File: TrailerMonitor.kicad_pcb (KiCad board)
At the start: 4 copper layers, 25 parts, among them U2 INA260AIPWR, U3 INA260AIPWR, U4 INA260AIPWR, U5 INA260AIPWR, U6 INA260AIPWR, U7 INA260AIPWR, U8 INA260AIPWR, U9 INA260AIPWR

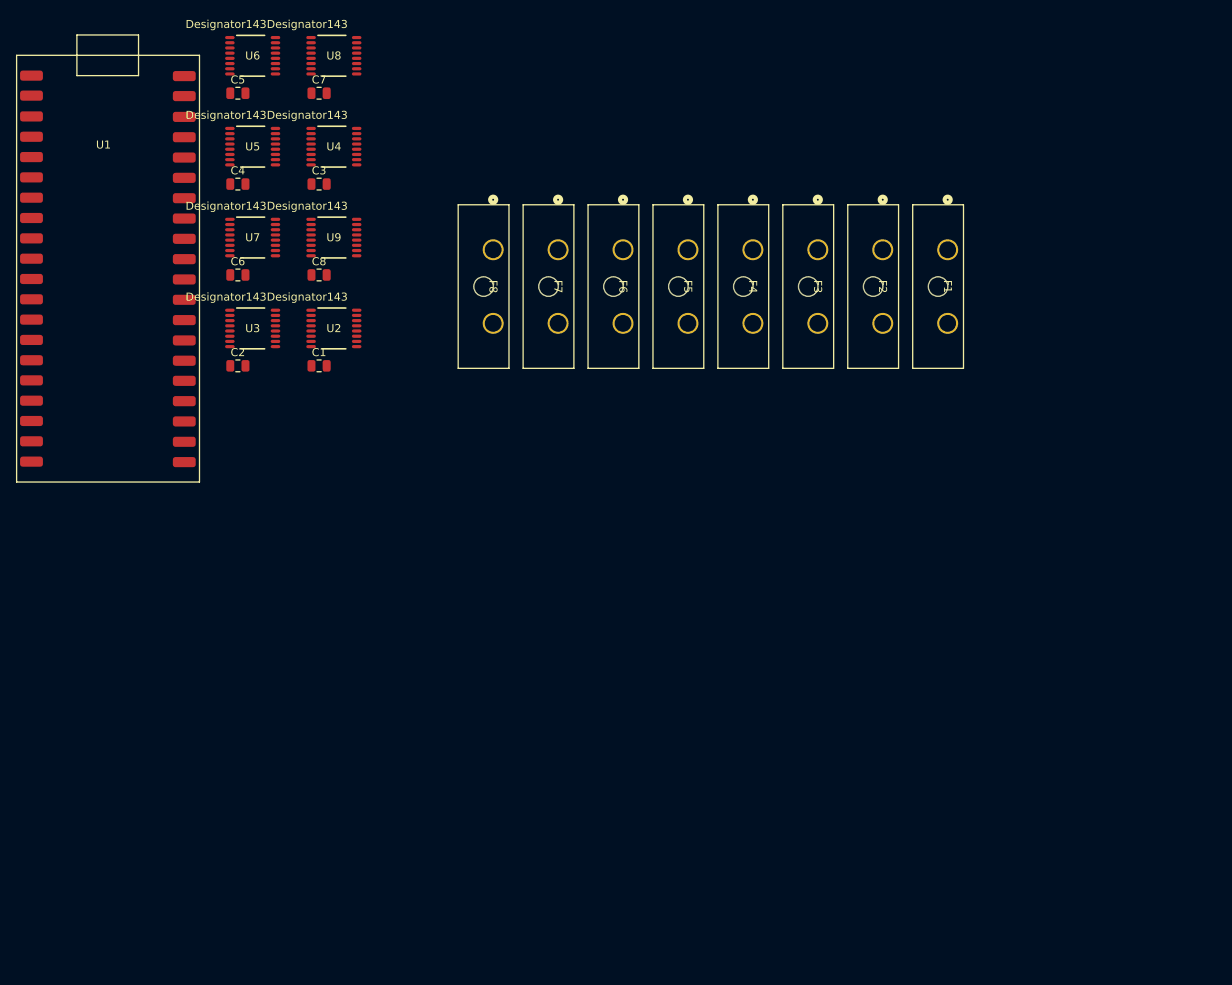
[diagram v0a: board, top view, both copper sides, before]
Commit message: Initial layout; remove INA260
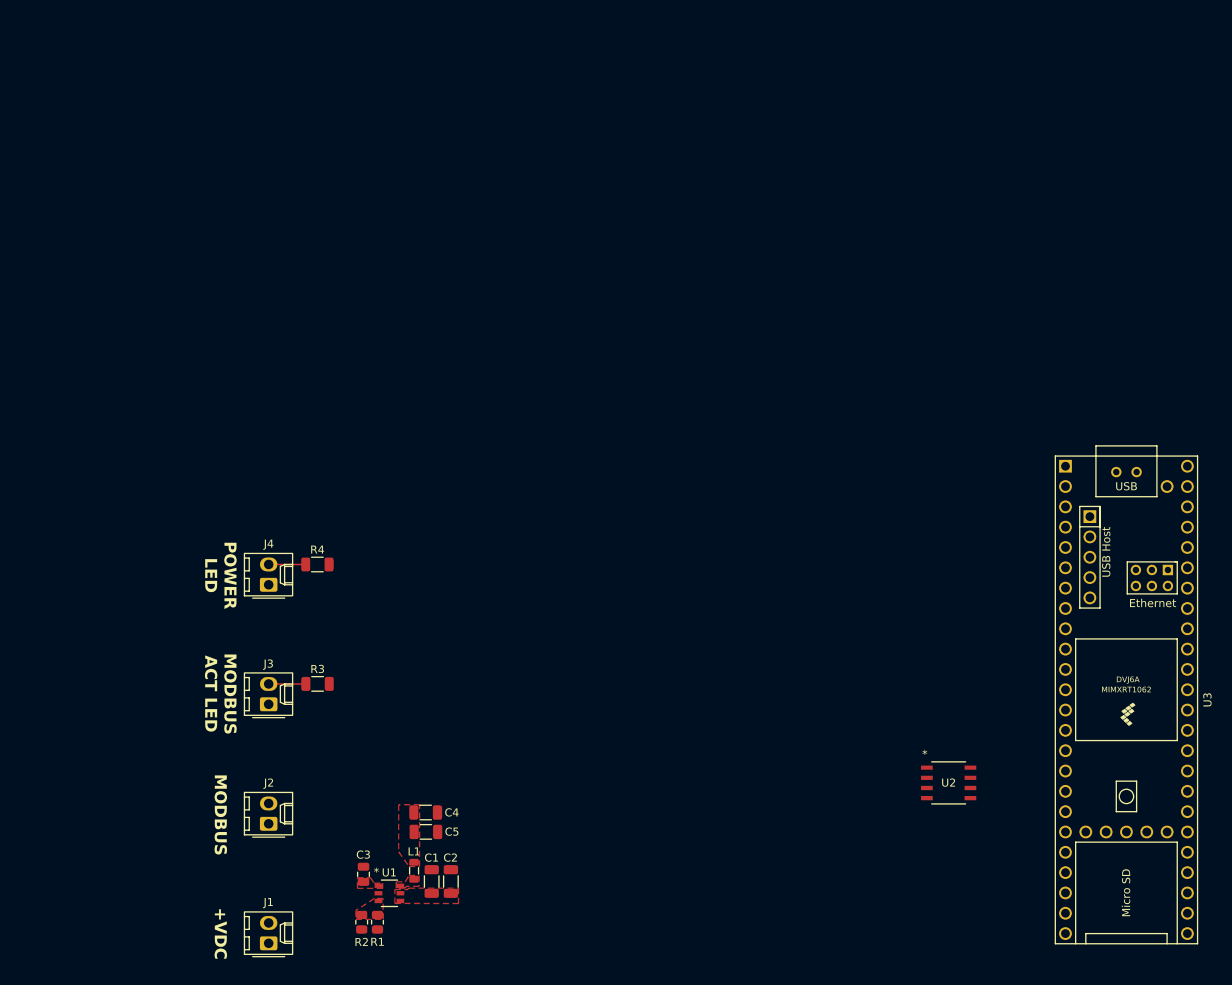
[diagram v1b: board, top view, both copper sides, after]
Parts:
- removed C6, C7, C8: 0.1u, Capacitor_SMD:C_0805_2012Metric
- removed F1, F2, F3, F4, F5, F6, F7, F8: 178.6164.0002, 178_6164_0002:FUSE_178-6164_LTF
- removed U4, U5, U6, U7, U8, U9: INA260AIPWR, INA260AIPWR:PW0016A_L
- added J1: +VIN (7-60 VDC), Connector_Molex:Molex_KK-254_AE-6410-02A_1x02_P2.54mm_Vertical, F.Cu at (153.9, 171.9)
- added J2: ModBus, Connector_Molex:Molex_KK-254_AE-6410-02A_1x02_P2.54mm_Vertical, F.Cu at (153.9, 157.0)
- added J3: LED (Power), Connector_Molex:Molex_KK-254_AE-6410-02A_1x02_P2.54mm_Vertical, F.Cu at (153.9, 142.0)
- added J4: LED (ModBus Act), Connector_Molex:Molex_KK-254_AE-6410-02A_1x02_P2.54mm_Vertical, F.Cu at (153.9, 127.1)
- added L1: 47u, Inductor_SMD:L_0805_2012Metric, F.Cu at (172.1, 162.8)
- added R1: 100k, Resistor_SMD:R_0805_2012Metric, F.Cu at (167.6, 169.3)
- added R2: 19k1, Resistor_SMD:R_0805_2012Metric, F.Cu at (165.6, 169.3)
- added R3: 160, Resistor_SMD:R_1206_3216Metric, F.Cu at (160.1, 139.5)
- added R4: 160, Resistor_SMD:R_1206_3216Metric, F.Cu at (160.0, 124.5)
- C1, C5: value 0.1u -> 4u7; footprint Capacitor_SMD:C_0805_2012Metric -> Capacitor_SMD:C_1206_3216Metric
- C2: value 0.1u -> 100n; footprint Capacitor_SMD:C_0805_2012Metric -> Capacitor_SMD:C_1206_3216Metric
- C3: value 0.1u -> 100n
- C4: value 0.1u -> 10u; footprint Capacitor_SMD:C_0805_2012Metric -> Capacitor_SMD:C_1206_3216Metric
- U1: value ~ -> LMR51606XDBVR; footprint rpi-pico2w:Raspberrypi pico2 w SMD -> LMR51606:SOT-23-6-DBV_TEX
- U2: value INA260AIPWR -> MAX485ESA+; footprint INA260AIPWR:PW0016A_L -> MAX485ESA:21-0041B_8_MXM
- U3: value INA260AIPWR -> Teensy4.1; footprint INA260AIPWR:PW0016A_L -> teensy:Teensy41
- moved U3 118.7 mm to (261.2, 141.5), turned to -90 degrees
- moved U2 95.6 mm to (238.9, 151.8)
- moved C5 95.3 mm to (173.6, 158.0)
- moved U1 92.4 mm to (169.0, 165.7)
- moved C3 86.5 mm to (165.8, 163.3), turned to -90 degrees
- moved C4 82.0 mm to (173.6, 155.6)
- moved C2 69.7 mm to (176.7, 164.2), turned to 90 degrees
- moved C1 66.0 mm to (174.3, 164.2), turned to 90 degrees
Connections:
- C1 pad 1: GND -> +VDC
- C1 pad 2: /INA260/SOURCE -> GND
- C2 pad 1: GND -> +VDC
- C2 pad 2: /INA261/SOURCE -> GND
- C3 pad 1: GND -> Net-(U1-SW)
- C3 pad 2: /INA262/SOURCE -> Net-(U1-CB)
- C4 pad 1: GND -> +5V
- C4 pad 2: /INA263/SOURCE -> GND
- C5 pad 1: GND -> +5V
- C5 pad 2: /INA264/SOURCE -> GND
- U1 pad 1: unconnected-(U1-GP0/I2C0_SDA/UART0_TX-Pad1) -> Net-(U1-CB)
- U1 pad 2: unconnected-(U1-GP1_/I2C0_SCL/UART0_RX-Pad2) -> GND
- U1 pad 3: GND -> Net-(U1-FB)
- U1 pad 4: unconnected-(U1-GP2/SPIO_SCK/I2C1_SDA-Pad4) -> +VDC
- U1 pad 5: unconnected-(U1-GP3/SPIO_TX/I2C1SCL-Pad5) -> +VDC
- U1 pad 6: unconnected-(U1-GP4/SPIO_RX/I2C0_SDA/_UART1_TX-Pad6) -> Net-(U1-SW)
- U2 pad 1: /INA260/SOURCE -> /RO
- U2 pad 2: /INA260/SOURCE -> /DE
- U2 pad 3: /INA260/SOURCE -> /DE
- U2 pad 4: /INA260/A1 -> /DI
- U2 pad 5: /INA260/A0 -> GND
- U2 pad 6: GND -> /A
- U2 pad 7: unconnected-(U2-ALERT-Pad7) -> /B
- U2 pad 8: /SDA0 -> +5V
- U3 pad 1: /INA261/SOURCE -> GND
- U3 pad 10: /INA261/SOURCE -> /DI
- U3 pad 11: GND -> unconnected-(U3-9_OUT1C-Pad11)
- U3 pad 12: /INA261/SOURCE -> unconnected-(U3-10_CS_MQSR-Pad12)
- U3 pad 14: /INA261/LOAD -> unconnected-(U3-12_MISO_MQSL-Pad14)
- U3 pad 15: /INA261/LOAD -> unconnected-(U3-3V3-Pad15)
- U3 pad 16: /INA261/LOAD -> unconnected-(U3-24_A10_TX6_SCL2-Pad16)
- U3 pad 2: /INA261/SOURCE -> unconnected-(U3-0_RX1_CRX2_CS1-Pad2)
- U3 pad 3: /INA261/SOURCE -> unconnected-(U3-1_TX1_CTX2_MISO1-Pad3)
- U3 pad 4: /INA261/A1 -> unconnected-(U3-2_OUT2-Pad4)
- U3 pad 5: /INA261/A0 -> unconnected-(U3-3_LRCLK2-Pad5)
- U3 pad 6: GND -> unconnected-(U3-4_BCLK2-Pad6)
- U3 pad 8: /SDA0 -> /DE
- U3 pad 9: /SCL0 -> /RO
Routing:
- net Net-(J4-Pin_2): track 0.00 -> 4.63 mm
- net Net-(J3-Pin_2): track 0.00 -> 4.43 mm
- added copper zone on F.Cu, net +5V
- added copper zone on F.Cu, net +VDC
- added copper zone on F.Cu, net Net-(U1-CB)
- added copper zone on F.Cu, net Net-(U1-FB)
- added copper zone on F.Cu, net Net-(U1-SW)
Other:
- board text added: "+VDC"
- board text added: "MODBUS"
- board text added: "MODBUS ACT LED"
- board text added: "POWER LED"

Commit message: Add VBUS/VSYS; final PCB layout
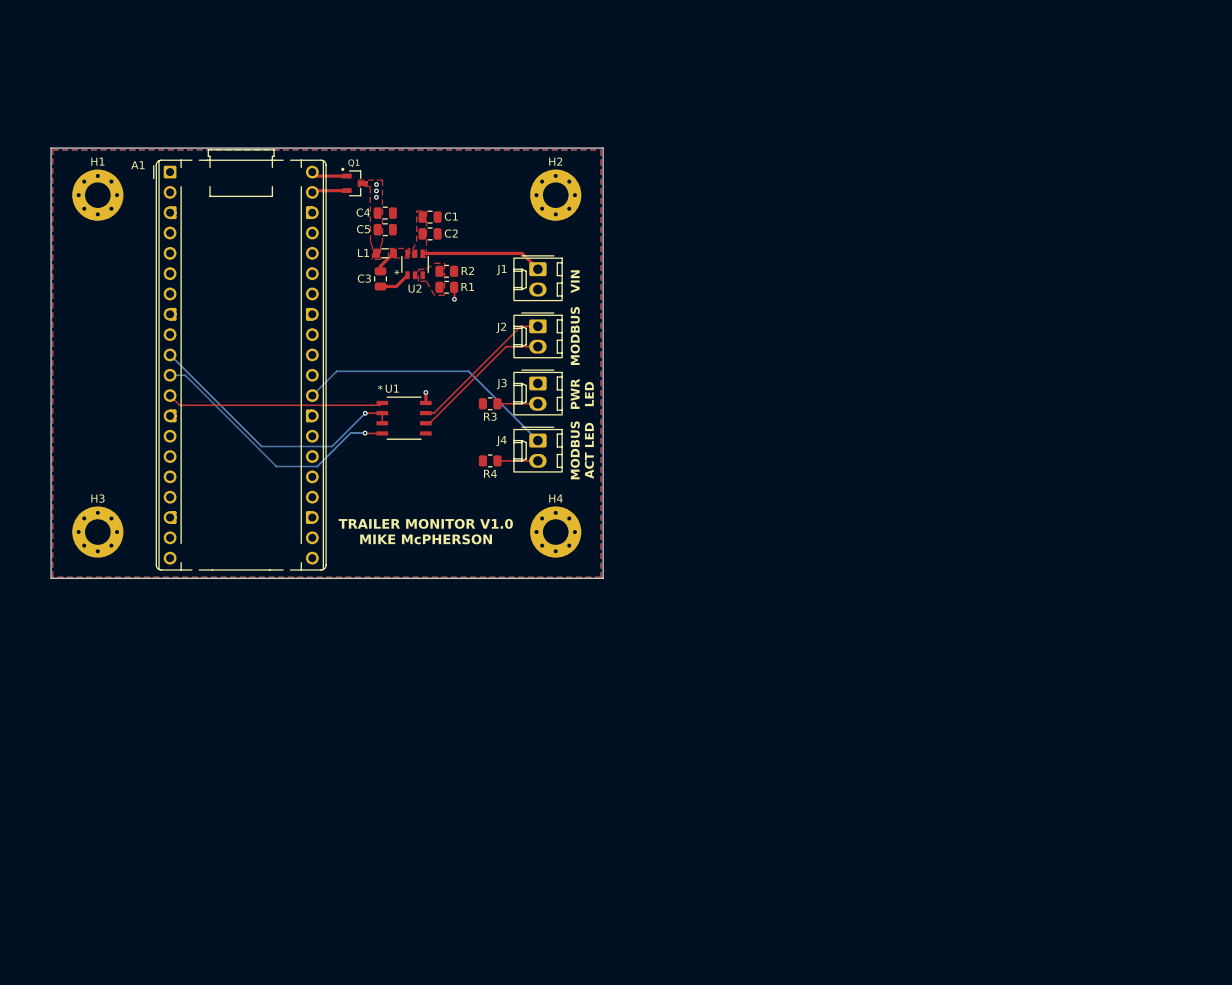
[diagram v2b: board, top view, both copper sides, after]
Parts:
- removed U3: Teensy4.1, teensy:Teensy41
- added A1: RaspberryPi_Pico_2W, Module:RaspberryPi_Pico_Common_THT, F.Cu at (141.6, 75.5)
- added H1: MountingHole_Pad, MountingHole:MountingHole_3.2mm_M3_Pad_Via, F.Cu at (132.6, 78.4)
- added H2: MountingHole_Pad, MountingHole:MountingHole_3.2mm_M3_Pad_Via, F.Cu at (189.8, 78.4)
- added H3: MountingHole_Pad, MountingHole:MountingHole_3.2mm_M3_Pad_Via, F.Cu at (132.6, 120.5)
- added H4: MountingHole_Pad, MountingHole:MountingHole_3.2mm_M3_Pad_Via, F.Cu at (189.8, 120.5)
- added Q1: DMG2305UX-13, DMG2305UX_13:SOT91P240X110-3N, F.Cu at (164.8, 76.9)
- C1, C2, C4, C5: footprint Capacitor_SMD:C_1206_3216Metric -> Capacitor_SMD:C_0805_2012Metric
- R3, R4: footprint Resistor_SMD:R_1206_3216Metric -> Resistor_SMD:R_0805_2012Metric
- U1: value LMR51606XDBVR -> MAX485ESA+; footprint LMR51606:SOT-23-6-DBV_TEX -> MAX485ESA:21-0041B_8_MXM
- U2: value MAX485ESA+ -> LMR51606XDBVR; footprint MAX485ESA:21-0041B_8_MXM -> LMR51606:SOT-23-6-DBV_TEX
- moved U2 93.0 mm to (172.3, 87.0), turned to 90 degrees
- moved J1 90.7 mm to (187.6, 87.6), turned to -90 degrees
- moved C1 83.1 mm to (174.1, 81.1), turned to 0 degrees
- moved R2 82.1 mm to (176.2, 87.9), turned to 0 degrees
- moved C2 81.0 mm to (174.1, 83.2), turned to 0 degrees
- moved R1 79.8 mm to (176.2, 89.9), turned to 180 degrees
- moved L1 77.3 mm to (168.5, 85.7), turned to 180 degrees
- moved C5 75.4 mm to (168.5, 82.7)
- moved C4 75.1 mm to (168.5, 80.6)
- moved C3 74.5 mm to (167.9, 88.8)
- moved J2 70.7 mm to (187.6, 94.8), turned to -90 degrees
- moved U1 59.4 mm to (170.9, 106.3)
- moved J3 52.4 mm to (187.6, 101.9), turned to -90 degrees
- moved R3 41.1 mm to (181.6, 104.5), turned to 180 degrees
- moved J4 38.2 mm to (187.6, 109.1), turned to -90 degrees
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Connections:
- C1 pad 1: +VDC -> Net-(J1-Pin_1)
- C2 pad 1: +VDC -> Net-(J1-Pin_1)
- C3 pad 1: Net-(U1-SW) -> Net-(U2-SW)
- C3 pad 2: Net-(U1-CB) -> Net-(U2-CB)
- J1 pad 1: +VDC -> Net-(J1-Pin_1)
- J2 pad 1: /A -> /B
- J2 pad 2: /B -> /A
- J4 pad 1: unconnected-(J4-Pin_1-Pad1) -> /MODBUS_ACT
- L1 pad 1: Net-(U1-SW) -> Net-(U2-SW)
- R1 pad 2: Net-(U1-FB) -> Net-(U2-FB)
- R2 pad 1: Net-(U1-FB) -> Net-(U2-FB)
- U1 pad 1: Net-(U1-CB) -> /RO
- U1 pad 2: GND -> /DE
- U1 pad 3: Net-(U1-FB) -> /DE
- U1 pad 4: +VDC -> /DI
- U1 pad 5: +VDC -> GND
- U1 pad 6: Net-(U1-SW) -> /A
- U2 pad 1: /RO -> Net-(U2-CB)
- U2 pad 2: /DE -> GND
- U2 pad 3: /DE -> Net-(U2-FB)
- U2 pad 4: /DI -> Net-(J1-Pin_1)
- U2 pad 5: GND -> Net-(J1-Pin_1)
- U2 pad 6: /A -> Net-(U2-SW)
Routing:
- net /DE: track 0.00 -> 34.4 mm, vias 0 -> 1
- net /MODBUS_ACT: track 0.00 -> 33.0 mm
- net /DI: track 0.00 -> 33.0 mm, vias 0 -> 1
- net /RO: track 0.00 -> 27.2 mm
- net /B: track 0.00 -> 18.5 mm
- net /A: track 0.00 -> 18.0 mm
- net Net-(J1-Pin_1): track 0.00 -> 15.2 mm
- net /VBUS: track 0.00 -> 4.53 mm
- net /VSYS: track 0.00 -> 4.41 mm
- net Net-(U2-CB): track 0.00 -> 3.95 mm
- net Net-(U2-SW): track 0.00 -> 2.92 mm
- net +5V: track 0.00 -> 2.83 mm, vias 0 -> 5
- net Net-(J3-Pin_2): track 4.43 -> 5.36 mm
- net Net-(J4-Pin_2): track 4.63 -> 5.16 mm
- added copper zone on B.Cu, net +5V
- added copper zone on F.Cu, net GND
- added copper zone on F.Cu, net Net-(J1-Pin_1)
- added copper zone on F.Cu, net Net-(U2-FB)
- added copper zone on F.Cu, net Net-(U2-SW)
- removed copper zone on F.Cu, net +VDC
- removed copper zone on F.Cu, net Net-(U1-CB)
- removed copper zone on F.Cu, net Net-(U1-FB)
- removed copper zone on F.Cu, net Net-(U1-SW)
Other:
- board outline added: 69 x 53.8 mm
- copper layers 4 -> 2
- board text added: "PWR LED"
- board text added: "TRAILER MONITOR V1.0 MIKE McPHERSON"
- board text added: "VIN"
- board text removed: "+VDC"
- board text removed: "POWER LED"
